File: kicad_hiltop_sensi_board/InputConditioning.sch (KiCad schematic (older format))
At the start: 23 parts, among them U4 AD8646, U5 AD8646

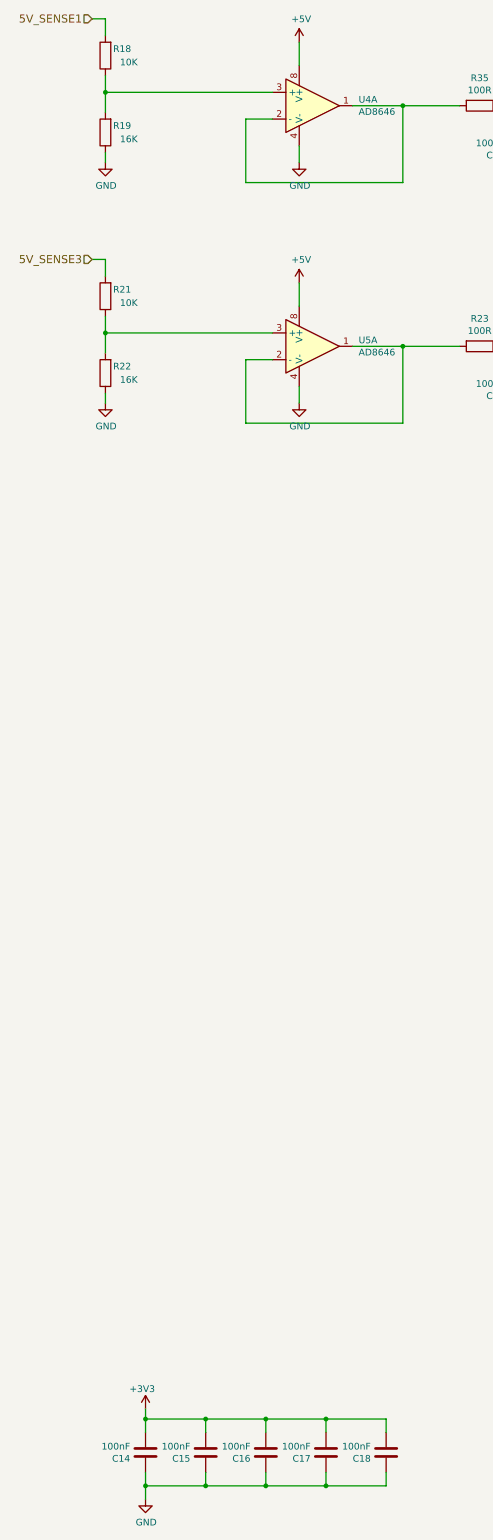
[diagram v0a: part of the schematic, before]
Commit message: LBBC sensi board upto date schematic and footprints
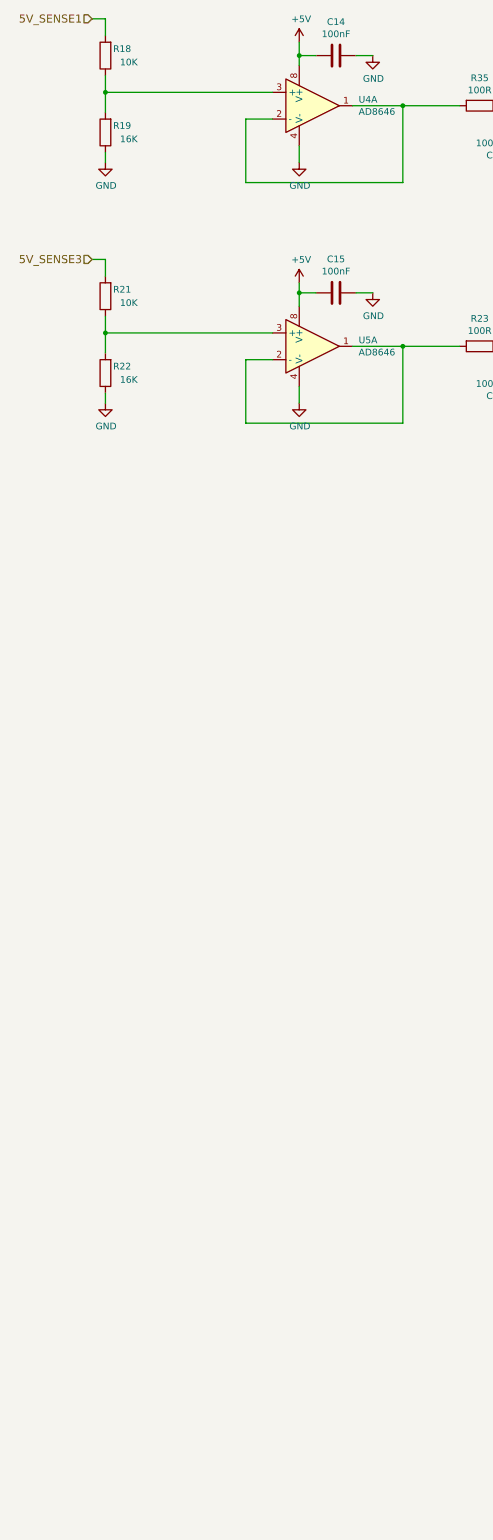
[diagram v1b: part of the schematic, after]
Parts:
- removed C14, C15, C16, C17, C18: 100nF, Capacitor_SMD:C_0603_1608Metric, symbol Sensi_Board-rescue:C-device
- added C14, C15: 100nF, Capacitor_SMD:C_0603_1608Metric, symbol device:C
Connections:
- net +5V: now also C14.2, C15.2
- net GND: now also C14.1, C15.1
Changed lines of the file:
@@
 $Descr A3 11693 16535 portrait
 encoding utf-8
-Sheet 2 11
+Sheet 11 11
 Title ""
 Date ""
@@
 Connection ~ 4725 3150
 $Comp
-L Sensi_Board-rescue:C-device C14
-U 1 1 5C4FA8D8
-P 1925 13225
-AR Path="/5BC9D0F6/5C4FA8D8" Ref="C14"  Part="1"
-AR Path="/5F14ACC5/5C4FA8D8" Ref="C?"  Part="1"
-F 0 "C14" H 2040 13271 50  0000 L CNN
-F 1 "100nF" H 2040 13180 50  0000 L CNN
-F 2 "Capacitor_SMD:C_0603_1608Metric" H 1963 13075 50  0001 C CNN
-F 3 "" H 1925 13225 50  0001 C CNN
-F 4 "105-002" H 0   0   50  0001 C CNN "Devtank"
-	1    1925 13225
-	-1   0    0    1
-$EndComp
-$Comp
-L Sensi_Board-rescue:C-device C15
-U 1 1 5C4FABED
-P 2375 13225
-AR Path="/5BC9D0F6/5C4FABED" Ref="C15"  Part="1"
-AR Path="/5F14ACC5/5C4FABED" Ref="C?"  Part="1"
-F 0 "C15" H 2490 13271 50  0000 L CNN
-F 1 "100nF" H 2490 13180 50  0000 L CNN
-F 2 "Capacitor_SMD:C_0603_1608Metric" H 2413 13075 50  0001 C CNN
-F 3 "" H 2375 13225 50  0001 C CNN
-F 4 "105-002" H 0   0   50  0001 C CNN "Devtank"
-	1    2375 13225
-	-1   0    0    1
-$EndComp
-$Comp
-L Sensi_Board-rescue:C-device C16
-U 1 1 5C4FAC61
-P 2825 13225
-AR Path="/5BC9D0F6/5C4FAC61" Ref="C16"  Part="1"
-AR Path="/5F14ACC5/5C4FAC61" Ref="C?"  Part="1"
-F 0 "C16" H 2940 13271 50  0000 L CNN
-F 1 "100nF" H 2940 13180 50  0000 L CNN
-F 2 "Capacitor_SMD:C_0603_1608Metric" H 2863 13075 50  0001 C CNN
-F 3 "" H 2825 13225 50  0001 C CNN
-F 4 "105-002" H 0   0   50  0001 C CNN "Devtank"
-	1    2825 13225
-	-1   0    0    1
-$EndComp
-$Comp
-L power:+3V3 #PWR049
-U 1 1 5C4FD83E
-P 1925 12900
-AR Path="/5BC9D0F6/5C4FD83E" Ref="#PWR049"  Part="1"
-AR Path="/5F14ACC5/5C4FD83E" Ref="#PWR?"  Part="1"
-F 0 "#PWR049" H 1925 12750 50  0001 C CNN
-F 1 "+3V3" H 1900 13050 50  0000 C CNN
-F 2 "" H 1925 12900 50  0001 C CNN
-F 3 "" H 1925 12900 50  0001 C CNN
-	1    1925 12900
-	1    0    0    -1
-$EndComp
-$Comp
-L power:GND #PWR050
-U 1 1 5C4FD9A5
-P 1925 13575
-AR Path="/5BC9D0F6/5C4FD9A5" Ref="#PWR050"  Part="1"
-AR Path="/5F14ACC5/5C4FD9A5" Ref="#PWR?"  Part="1"
-F 0 "#PWR050" H 1925 13325 50  0001 C CNN
-F 1 "GND" H 1930 13402 50  0000 C CNN
-F 2 "" H 1925 13575 50  0001 C CNN
-F 3 "" H 1925 13575 50  0001 C CNN
-	1    1925 13575
-	1    0    0    -1
-$EndComp
-$Comp
 L Sensi_Board-rescue:R-device R18
 U 1 1 5C7680D6
@@
 	1525 2500 1625 2500
 $Comp
-L Sensi_Board-rescue:C-device C17
-U 1 1 5C809382
-P 3275 13225
-AR Path="/5BC9D0F6/5C809382" Ref="C17"  Part="1"
-AR Path="/5F14ACC5/5C809382" Ref="C?"  Part="1"
-F 0 "C17" H 3390 13271 50  0000 L CNN
-F 1 "100nF" H 3390 13180 50  0000 L CNN
-F 2 "Capacitor_SMD:C_0603_1608Metric" H 3313 13075 50  0001 C CNN
-F 3 "" H 3275 13225 50  0001 C CNN
-F 4 "105-002" H 0   0   50  0001 C CNN "Devtank"
-	1    3275 13225
-	-1   0    0    1
-$EndComp
-$Comp
-L Sensi_Board-rescue:C-device C18
-U 1 1 5C80943A
-P 3725 13225
-AR Path="/5BC9D0F6/5C80943A" Ref="C18"  Part="1"
-AR Path="/5F14ACC5/5C80943A" Ref="C?"  Part="1"
-F 0 "C18" H 3840 13271 50  0000 L CNN
-F 1 "100nF" H 3840 13180 50  0000 L CNN
-F 2 "Capacitor_SMD:C_0603_1608Metric" H 3763 13075 50  0001 C CNN
-F 3 "" H 3725 13225 50  0001 C CNN
-F 4 "105-002" H 0   0   50  0001 C CNN "Devtank"
-	1    3725 13225
-	-1   0    0    1
-$EndComp
-Wire Wire Line
-	3725 13075 3725 12975
-Wire Wire Line
-	3725 12975 3275 12975
-Wire Wire Line
-	1925 12975 1925 12900
-Wire Wire Line
-	1925 13075 1925 12975
-Connection ~ 1925 12975
-Wire Wire Line
-	2375 13075 2375 12975
-Connection ~ 2375 12975
-Wire Wire Line
-	2375 12975 1925 12975
-Wire Wire Line
-	2825 13075 2825 12975
-Connection ~ 2825 12975
-Wire Wire Line
-	2825 12975 2375 12975
-Wire Wire Line
-	3275 13075 3275 12975
-Connection ~ 3275 12975
-Wire Wire Line
-	3275 12975 2825 12975
-Wire Wire Line
-	1925 13375 1925 13475
-Wire Wire Line
-	2375 13375 2375 13475
-Connection ~ 1925 13475
-Wire Wire Line
-	1925 13475 1925 13575
-Wire Wire Line
-	2825 13375 2825 13475
-Wire Wire Line
-	1925 13475 2375 13475
-Connection ~ 2375 13475
-Wire Wire Line
-	2375 13475 2825 13475
-Wire Wire Line
-	3275 13375 3275 13475
-Wire Wire Line
-	3275 13475 2825 13475
-Connection ~ 2825 13475
-Wire Wire Line
-	3725 13375 3725 13475
-Wire Wire Line
-	3725 13475 3275 13475
-Connection ~ 3275 13475
-$Comp
 L Devtank:AD8646 U4
 U 2 1 5FB049D9
@@
 $EndComp
 Wire Wire Line
-	3075 2850 3075 2675
+	3075 2850 3075 2775
 Wire Wire Line
 	3075 3450 3075 3575
@@
 $EndComp
 Wire Wire Line
-	3075 4650 3075 4475
-Wire Wire Line
 	3075 5250 3075 5375
 Text HLabel 6525 4450 0    60   Input ~ 0
@@
 Wire Wire Line
 	8075 5400 8075 5525
+$Comp
+L device:C C14
+U 1 1 5DB1A4DE
+P 3350 2775
+F 0 "C14" V 3098 2775 50  0000 C CNN
+F 1 "100nF" V 3189 2775 50  0000 C CNN
+F 2 "Capacitor_SMD:C_0603_1608Metric" H 3388 2625 50  0001 C CNN
+F 3 "" H 3350 2775 50  0001 C CNN
+	1    3350 2775
+	0    1    1    0
+$EndComp
+$Comp
+L power:GND #PWR05
+U 1 1 5DB1AD38
+P 3625 2775
+F 0 "#PWR05" H 3625 2525 50  0001 C CNN
+F 1 "GND" H 3630 2602 50  0000 C CNN
+F 2 "" H 3625 2775 50  0001 C CNN
+F 3 "" H 3625 2775 50  0001 C CNN
+	1    3625 2775
+	1    0    0    -1
+$EndComp
+Wire Wire Line
+	3200 2775 3075 2775
+Connection ~ 3075 2775
+Wire Wire Line
+	3075 2775 3075 2675
+Wire Wire Line
+	3500 2775 3625 2775
+$Comp
+L device:C C15
+U 1 1 5DB2F1B3
+P 3350 4550
+F 0 "C15" V 3098 4550 50  0000 C CNN
+F 1 "100nF" V 3189 4550 50  0000 C CNN
+F 2 "Capacitor_SMD:C_0603_1608Metric" H 3388 4400 50  0001 C CNN
+F 3 "" H 3350 4550 50  0001 C CNN
+	1    3350 4550
+	0    1    1    0
+$EndComp
+$Comp
+L power:GND #PWR06
+U 1 1 5DB2F1B9
+P 3625 4550
+F 0 "#PWR06" H 3625 4300 50  0001 C CNN
+F 1 "GND" H 3630 4377 50  0000 C CNN
+F 2 "" H 3625 4550 50  0001 C CNN
+F 3 "" H 3625 4550 50  0001 C CNN
+	1    3625 4550
+	1    0    0    -1
+$EndComp
+Wire Wire Line
+	3200 4550 3075 4550
+Wire Wire Line
+	3500 4550 3625 4550
+Wire Wire Line
+	3075 4475 3075 4550
+Wire Wire Line
+	3075 4550 3075 4650
+Connection ~ 3075 4550
 $EndSCHEMATC
